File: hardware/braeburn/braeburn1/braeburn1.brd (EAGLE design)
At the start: 100 x 70.5 mm, 49 parts, among them IC1 MAX481CSA, IC2 MEGA8-AI, IC3 LM324D, IC4 LM2574N-12, IC5 LM2574N-5.0, IC6 LM2574N-3.3, Q1 20MHz

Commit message: improvements on the design
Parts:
- R16: value (none) -> 270Ohm
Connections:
- net OUT_3V3: no longer R16.1
- net OUT_5V: now also R16.1
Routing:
- net OUT_5V: track 168.8 -> 239.5 mm, vias 4 -> 6
- net OUT_3V3: track 276.4 -> 249.6 mm
- net GND: track 520.1 -> 509.6 mm, vias 24 -> 26

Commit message: removed airwire.
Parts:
- added D4: 1N400X, diode:DO41-10
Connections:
- new net N$15: D4.A, J2.3
- net DCIN: now also D4.C; no longer J2.3
- net GND: no longer U$1.B09(GND)
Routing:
- net GND: track 509.6 -> 516.0 mm, vias 26 -> 29
- net N$15: track 0.00 -> 3.51 mm
- net OUT_5V: track 239.5 -> 236.4 mm
- net DCIN: track 98.0 -> 95.3 mm
- net OUT_3V3: track 249.6 -> 250.3 mm
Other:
- board text added: "braeburn v1"
- board text added: "cc-by-nc-sa"

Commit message: .
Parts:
- R16: value 270Ohm -> 330Ohm
- moved R16 0.98 mm to (57.6, 64.5)
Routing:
- net OUT_5V: track 236.4 -> 235.4 mm
- net N$18: track 3.05 -> 4.02 mm
- net OUT_3V3: track 250.3 -> 249.7 mm
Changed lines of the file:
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@@
 <layer number="42" name="bRestrict" color="1" fill="10" visible="no" active="yes"/>
 <layer number="43" name="vRestrict" color="2" fill="10" visible="no" active="yes"/>
-<layer number="44" name="Drills" color="7" fill="1" visible="no" active="yes"/>
-<layer number="45" name="Holes" color="7" fill="1" visible="no" active="yes"/>
-<layer number="46" name="Milling" color="3" fill="1" visible="no" active="yes"/>
-<layer number="47" name="Measures" color="7" fill="1" visible="no" active="yes"/>
-<layer number="48" name="Document" color="7" fill="1" visible="no" active="yes"/>
-<layer number="49" name="Reference" color="7" fill="1" visible="no" active="yes"/>
-<layer number="51" name="tDocu" color="7" fill="1" visible="no" active="yes"/>
-<layer number="52" name="bDocu" color="7" fill="1" visible="no" active="yes"/>
+<layer number="44" name="Drills" color="7" fill="1" visible="yes" active="yes"/>
+<layer number="45" name="Holes" color="7" fill="1" visible="yes" active="yes"/>
+<layer number="46" name="Milling" color="3" fill="1" visible="yes" active="yes"/>
+<layer number="47" name="Measures" color="7" fill="1" visible="yes" active="yes"/>
+<layer number="48" name="Document" color="7" fill="1" visible="yes" active="yes"/>
+<layer number="49" name="Reference" color="7" fill="1" visible="yes" active="yes"/>
+<layer number="51" name="tDocu" color="7" fill="1" visible="yes" active="yes"/>
+<layer number="52" name="bDocu" color="7" fill="1" visible="yes" active="yes"/>
 <layer number="91" name="Nets" color="2" fill="1" visible="no" active="no"/>
 <layer number="92" name="Busses" color="1" fill="1" visible="no" active="no"/>
@@
 <text x="12.95" y="69.3" size="1.778" layer="1">braeburn v1</text>
 <text x="34.175" y="69.35" size="1.778" layer="1">cc-by-nc-sa</text>
+<hole x="2.1" y="6.375" drill="2"/>
+<hole x="2.2" y="72.175" drill="2"/>
 </plain>
 <attributes>
@@
 <element name="R15" library="rcl" package="R0603" value="10K" x="75.755" y="67.04"/>
 <element name="PWRLED" library="pinhead" package="1X02" value="" x="55.43" y="68.57"/>
-<element name="R16" library="rcl" package="R0603" value="270Ohm" x="57.595" y="65.525" rot="R180"/>
+<element name="R16" library="rcl" package="R0603" value="330Ohm" x="57.595" y="64.55" rot="R180"/>
 <element name="L1" library="rcl" package="0207/5V" value="" x="80.74" y="36.55" rot="R180"/>
 <element name="IC4" library="linear" package="DIL08" value="LM2574N-12" x="46.38" y="48.925" rot="R90"/>
@@
 <wire x1="13.585" y1="26.64" x2="13.375" y2="26.85" width="1.016" layer="1"/>
 <wire x1="13.41" y1="12.93" x2="13.41" y2="11.19" width="1.27" layer="1"/>
-<wire x1="13.41" y1="11.19" x2="17.475" y2="7.125" width="1.27" layer="1"/>
-<via x="17.475" y="7.125" extent="1-16" drill="0.5" shape="square"/>
-<wire x1="17.475" y1="7.125" x2="33.2" y2="7.125" width="1.27" layer="16"/>
-<wire x1="33.2" y1="7.125" x2="39.475" y2="13.4" width="1.27" layer="16"/>
+<wire x1="13.41" y1="11.19" x2="16.8" y2="7.875" width="1.27" layer="1"/>
+<via x="16.8" y="7.875" extent="1-16" drill="0.5" shape="square"/>
+<wire x1="16.8" y1="7.875" x2="33.925" y2="7.875" width="1.27" layer="16"/>
+<wire x1="33.925" y1="7.875" x2="39.475" y2="13.4" width="1.27" layer="16"/>
 <wire x1="39.475" y1="13.4" x2="45.35" y2="13.375" width="1.27" layer="16"/>
 <wire x1="45.35" y1="13.375" x2="47.625" y2="11.375" width="1.27" layer="16"/>
@@
 <wire x1="52.435" y1="1.485" x2="52.435" y2="1.46" width="0.6096" layer="16"/>
 <contactref element="R16" pad="1"/>
-<wire x1="58.445" y1="65.525" x2="58.575" y2="65.395" width="0.4064" layer="1"/>
-<wire x1="58.575" y1="65.395" x2="58.575" y2="45.625" width="0.4064" layer="1"/>
+<wire x1="58.445" y1="64.55" x2="58.575" y2="64.345" width="0.4064" layer="1"/>
+<wire x1="58.575" y1="64.345" x2="58.575" y2="45.625" width="0.4064" layer="1"/>
 <via x="58.575" y="45.625" extent="1-16" drill="0.9" shape="square"/>
 <wire x1="58.575" y1="45.625" x2="55.875" y2="42.925" width="0.4064" layer="16"/>
@@
 <contactref element="PWRLED" pad="2"/>
 <wire x1="56.7" y1="68.57" x2="56.745" y2="68.35" width="0.6096" layer="1"/>
-<wire x1="56.745" y1="68.35" x2="56.745" y2="65.525" width="0.6096" layer="1"/>
+<wire x1="56.745" y1="68.35" x2="56.745" y2="64.55" width="0.6096" layer="1"/>
 </signal>
 <signal name="DCIN">

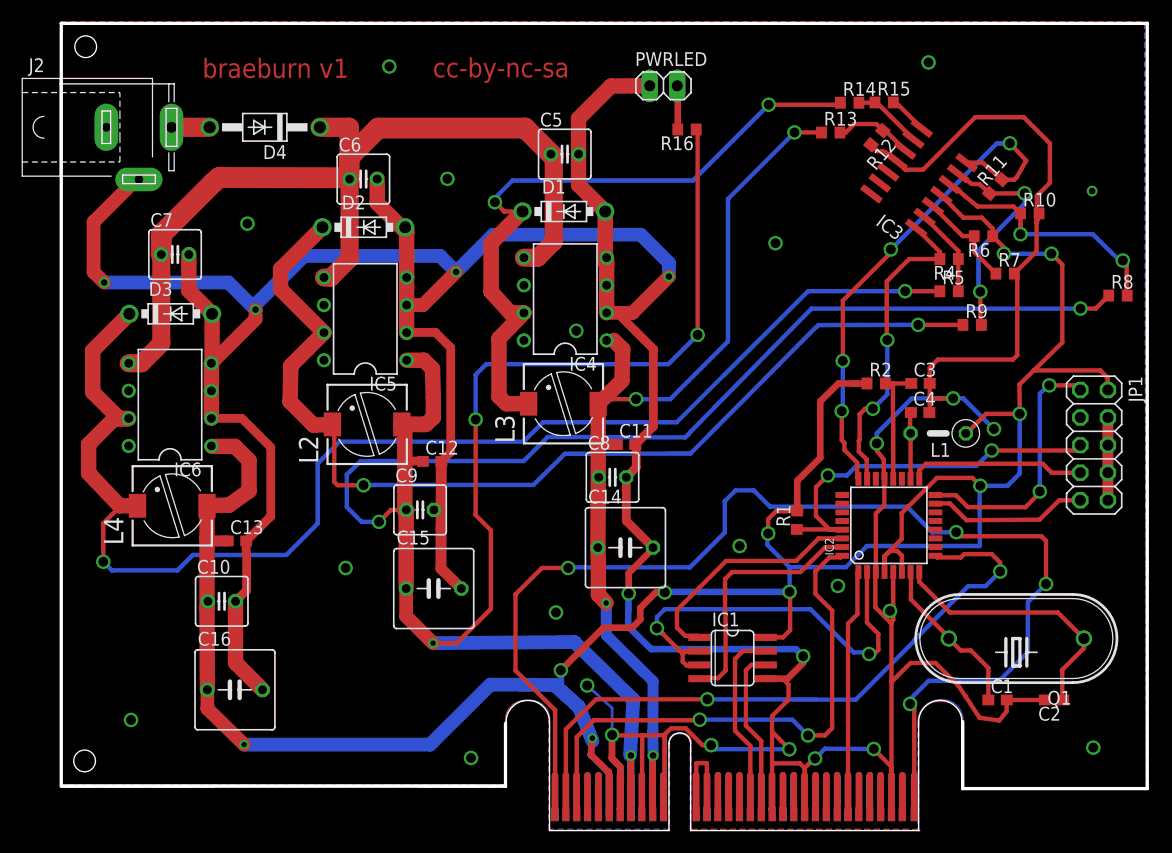
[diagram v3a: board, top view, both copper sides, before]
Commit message: some traces of braeburn1 are 20% cooler now
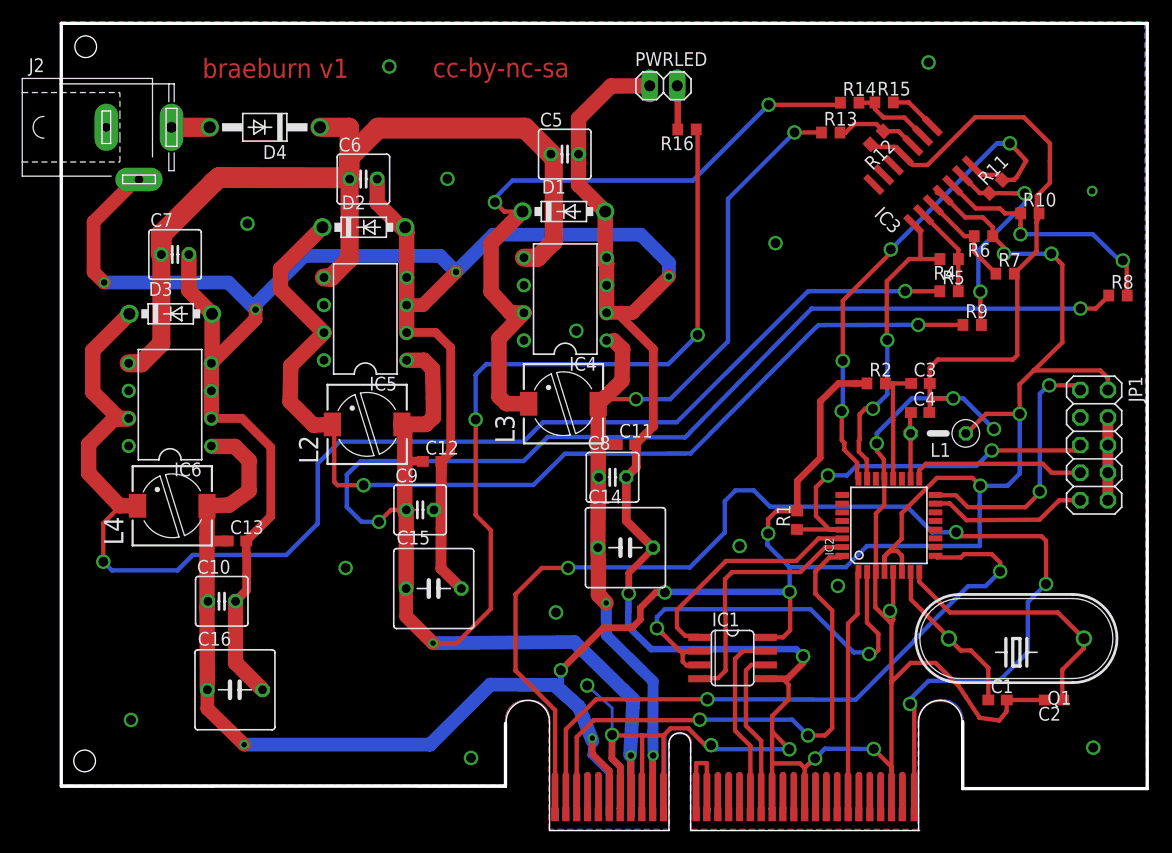
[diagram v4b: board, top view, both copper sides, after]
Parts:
- moved IC3 0.47 mm to (79.3, 60.3), turned to 45 degrees
- turned R11 to 45 degrees
- turned R12 to 225 degrees
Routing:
- net N$21: track 6.43 -> 7.66 mm
- net M_12V: track 3.61 -> 4.74 mm
- net GND: track 516.0 -> 515.2 mm
- net N$20: track 7.31 -> 8.05 mm
- net M5V: track 48.1 -> 47.5 mm
